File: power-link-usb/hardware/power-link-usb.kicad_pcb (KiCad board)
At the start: 4 copper layers, 50 x 34.5 mm, 30 parts, among them J1 >VALUE, J102 DX07S016JA3, J103 NE8FAH, J104 NE8FAH, Q101 BSC010N04LS, Q102 BSC010N04LS, U101 CYPM1311-48LDXI

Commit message: Update power-link-usb
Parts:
- J1: value >VALUE -> KitProg3
- moved C107 0.75 mm to (159.2, 112.5)
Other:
- board text added: "2026-01-28 stencil 2026-02-10 Move C107 out of the way"

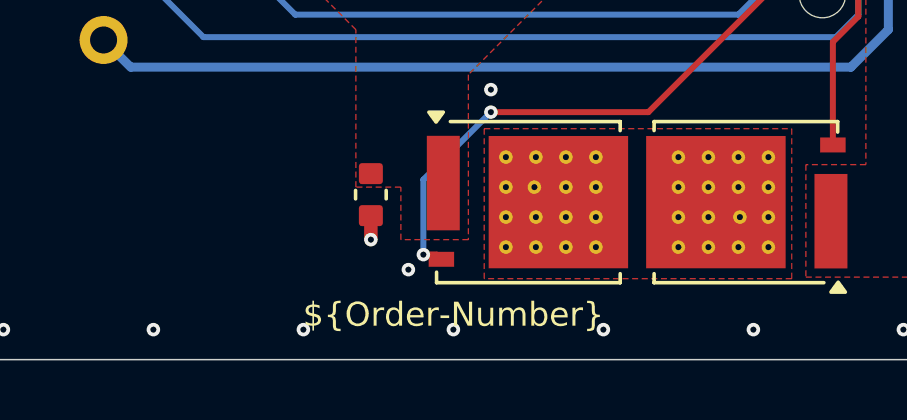
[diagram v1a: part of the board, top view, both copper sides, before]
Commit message: Replace Order_Number
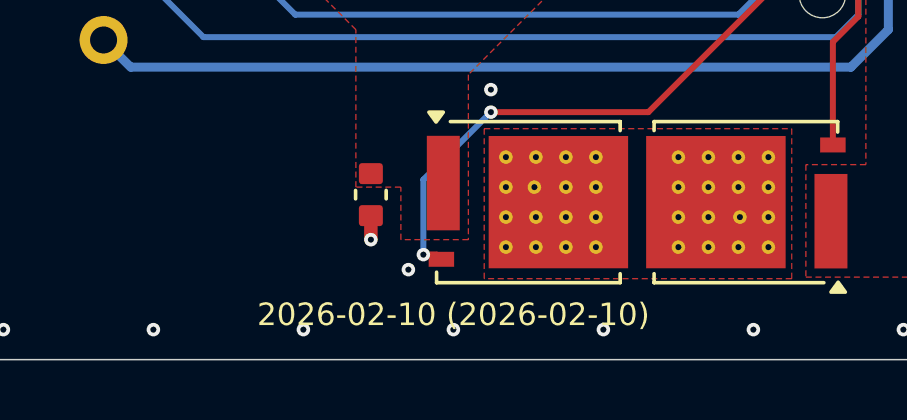
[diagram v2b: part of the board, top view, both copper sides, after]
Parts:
- INFO101: value Order_Number -> ~; footprint V2_Production:Order_Number -> V2_Production:Revision
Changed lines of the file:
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@@
 		)
 	)
-	(property "Order-Number" "JLCJLCJLCJLC")
 	(net 0 "")
 	(net 1 "GND")
@@
 		)
 	)
-	(footprint "V2_Production:Order_Number"
+	(footprint "V2_Production:Revision"
 		(layer "F.Cu")
 		(at 142 115.5)
@@
 			)
 		)
-		(property "Value" "Order_Number"
+		(property "Value" "~"
 			(at 0 2.27 0)
 			(unlocked yes)
@@
 		(sheetname "/")
 		(sheetfile "power-link-usb.kicad_sch")
-		(attr exclude_from_pos_files exclude_from_bom)
-		(fp_rect
-			(start -7 -0.75)
-			(end 7 0.75)
-			(stroke
-				(width 0.05)
-				(type default)
+		(attr exclude_from_pos_files exclude_from_bom allow_missing_courtyard)
+		(fp_text user "${REVISION} (${ISSUE_DATE})"
+			(at 0 0 0)
+			(unlocked yes)
+			(layer "F.SilkS")
+			(effects
+				(font
+					(size 0.75 0.75)
+					(thickness 0.1)
+				)
 			)
-			(fill no)
-			(layer "F.CrtYd")
 		)
-		(fp_text user "${Order-Number}"
+		(fp_text user "${REVISION} (${ISSUE_DATE})"
 			(at 0 0 0)
 			(unlocked yes)
-			(layer "F.SilkS")
+			(layer "F.Fab")
 			(effects
 				(font
-					(size 0.8 0.8)
-					(thickness 0.12)
+					(size 0.75 0.75)
+					(thickness 0.1)
 				)
 			)
@@
 					(thickness 0.15)
 				)
-			)
-		)
-		(property "Sim.Enable" "0"
-			(at 0 0 0)
-			(unlocked yes)
-			(layer "F.Fab")
-			(hide yes)
-			(effects
-				(font
-					(size 1 1)
-					(thickness 0.15)
-				)

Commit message: Export stencil
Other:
- board text removed: "2026-01-28 stencil 2026-02-10 Move C107 out of the way"
